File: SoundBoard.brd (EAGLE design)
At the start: 14.2 x 23.4 mm, 17 parts, among them IC1 LMV324, U1 ADMP401

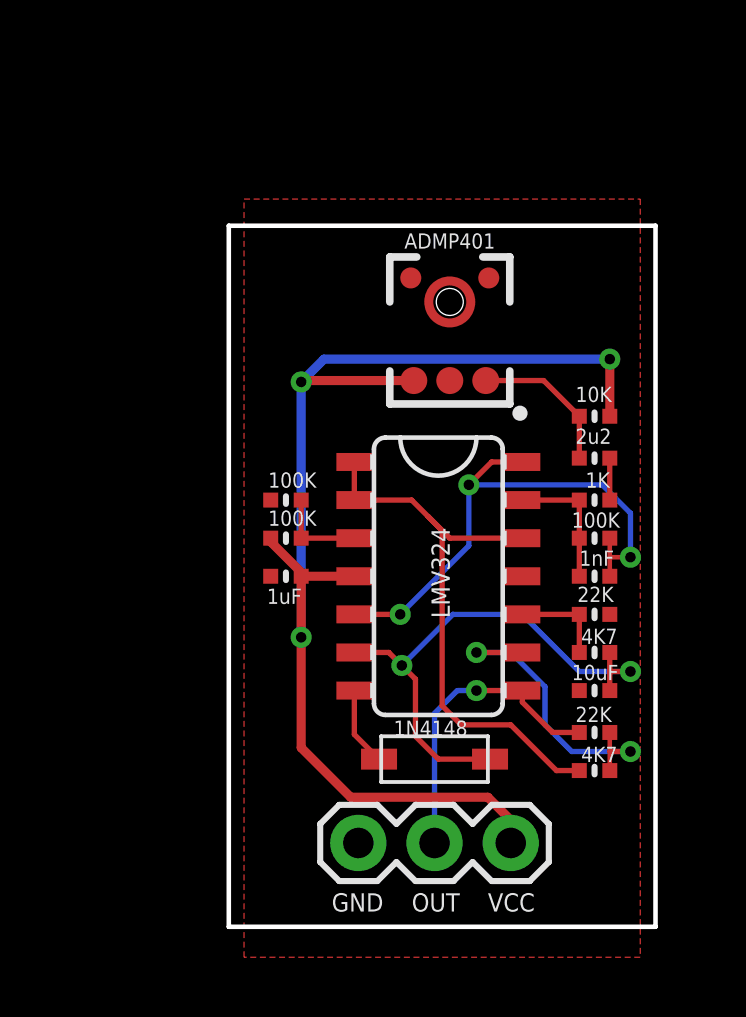
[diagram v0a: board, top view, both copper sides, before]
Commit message: v2 - updated OPAMP to LM324QT
- rerouted traces to accomodate for new QFN part
- Added electret microphone pins to test both
- rearranged some parts
- increased board dimensions slightly
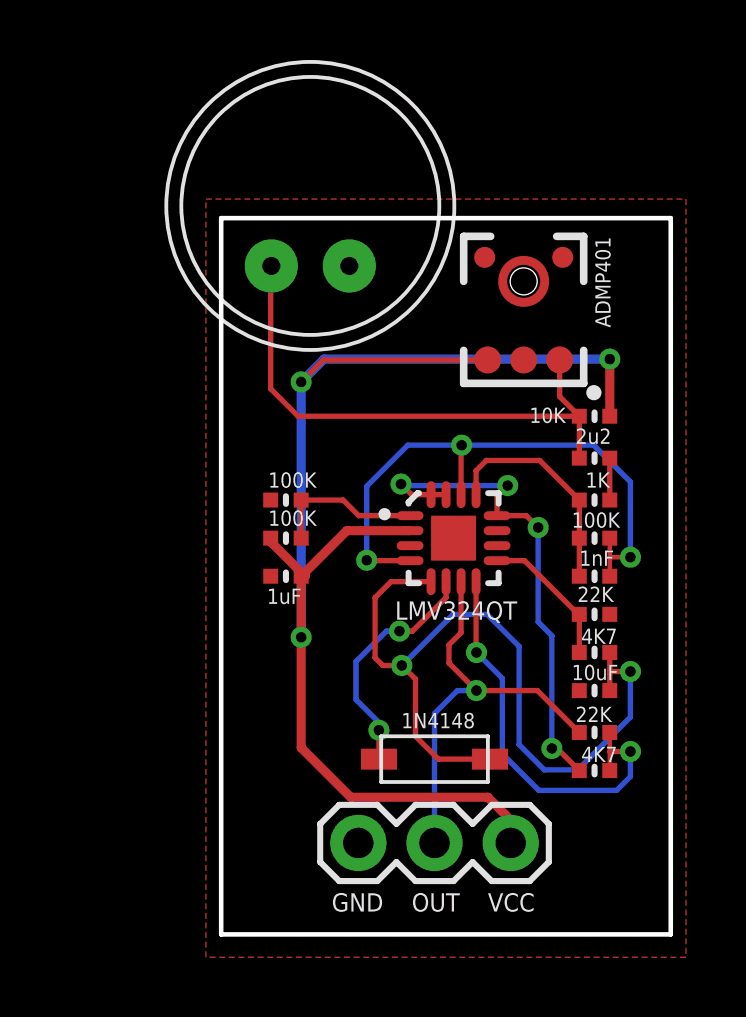
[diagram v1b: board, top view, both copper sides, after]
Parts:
- removed IC1: LMV324, SparkFun-AnalogIC:SO014
- added Q1: (no value), adafruit:9.7ELECTRET
- added U$1: LMV324QT, LMV324:QFN-16_3X3
- moved U1 2.56 mm to (12.9, 23.8)
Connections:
- net AMP: now also U$1.14, U$1.4; no longer IC1.14, IC1.5
- net GND: now also Q1.-, U$1.11; no longer IC1.11
- net N$2: now also U$1.13; no longer IC1.13
- net N$3: now also Q1.+
- net N$4: now also U$1.9; no longer IC1.10
- net N$5: now also U$1.8; no longer IC1.9
- net N$6: now also U$1.6; no longer IC1.7
- net N$7: now also U$1.5; no longer IC1.6
- net N$9: now also U$1.1; no longer IC1.3
- net OUT: now also U$1.7; no longer IC1.8
- net VCC: now also U$1.2; no longer IC1.4
- net VCC/2: now also U$1.12, U$1.15, U$1.16; no longer IC1.1, IC1.12, IC1.2
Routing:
- net N$3: track 5.01 -> 18.3 mm
- net N$7: track 18.2 -> 27.0 mm
- net VCC: track 42.8 -> 48.1 mm
- net N$6: track 2.63 -> 7.98 mm, vias 0 -> 2
- net OUT: track 10.3 -> 14.2 mm
- net N$5: track 10.7 -> 13.9 mm
- net N$2: track 4.44 -> 7.47 mm
- net VCC/2: track 19.4 -> 16.7 mm, vias 0 -> 4
- net N$9: track 3.04 -> 5.12 mm
- net AMP: track 18.1 -> 19.9 mm
- net N$4: track 3.17 -> 4.77 mm
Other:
- board size 14.2 x 23.4 mm -> 15 x 23.9 mm
- board text added: "Sound Board v2"
- board text removed: "LMV324"
- board text removed: "Sound Board"

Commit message: v3 - replaced MEMS mic with electret mic (adjusted circuitry)
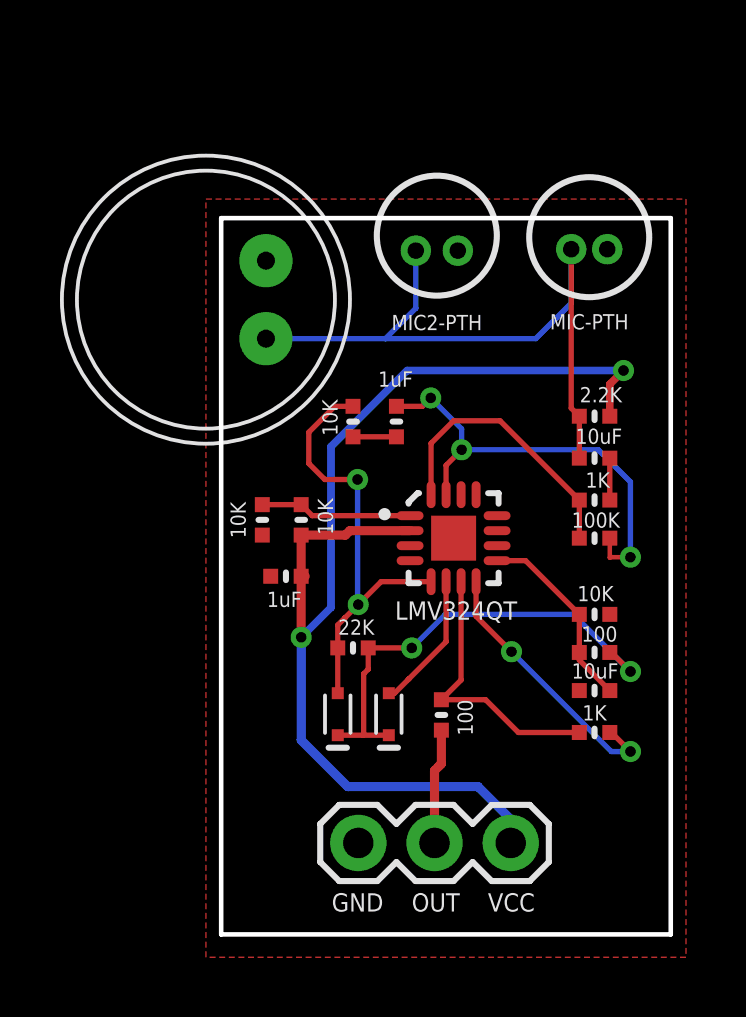
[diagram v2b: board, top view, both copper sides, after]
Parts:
- removed D1: 1N4148, adafruit:SOD-123
- removed U1: ADMP401, SparkFun-Sensors:ADMP401
- added D3, D4: 120mA/40V/370mV, SparkFun-DiscreteSemi:SOD-523
- added MK1: MIC2-PTH, CMC-4015-40P:MICROPHONE-PTH-4.0MM
- added MK2: MIC-PTH, TOM-1545P-R:MICROPHONE-PTH-4.0MM
- added R10: 10K, Adafruit PowerBoost 1000C Rev B:MICROBUILDER__0402MP
- added R11: 22K, Adafruit PowerBoost 1000C Rev B:MICROBUILDER__0402MP
- C1: value 2u2 -> 10uF
- C2: value 1nF -> 1uF
- R2: value 10K -> 2.2K
- R4, R6: value 4K7 -> 100
- R5: value 22K -> 10K
- R7: value 22K -> 1K
- R8, R9: value 100K -> 10K
- moved C2 8.38 mm to (8.64, 19.1), turned to 270 degrees
- moved R6 5.43 mm to (10.1, 9.35), turned to 90 degrees
- moved Q1 4.68 mm to (2.29, 23.2), turned to 270 degrees
- moved R8 1.00 mm to (4.17, 15.8), turned to 90 degrees
- moved R9 0.83 mm to (5.46, 15.8), turned to 270 degrees
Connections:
- removed net N$3: C1.1, Q1.+, R2.1, U1.1
- new net N$10: C1.1, MK1.OUT, MK2.OUT, Q1.+, R2.1
- new net N$8: C2.2, R10.2
- new net _OUT: R6.2, R7.1, U$1.7
- net AMP: now also C2.1, U$1.15; no longer C2.2, U$1.14, U$1.4
- net GND: now also MK1.GND, MK2.GND, R8.1, U$1.4; no longer R9.2, U1.2, U1.4, U1.6
- net N$2: now also U$1.16; no longer C2.1, U$1.13
- net N$4: now also D4.A, U$1.6; no longer R4.2, R5.2, U$1.9
- net N$5: no longer R6.1
- net N$6: now also D3.A, R10.1, R11.2, U$1.5; no longer D1.A, U$1.6
- net N$7: now also D3.C, D4.C, R11.1; no longer C3.2, D1.C, U$1.5
- net N$9: now also C3.2, R4.2, R5.2, U$1.9; no longer R8.2, R9.1, U$1.1
- net OUT: now also R6.1; no longer R7.1, U$1.7
- net VCC: now also R9.2; no longer R8.1, U1.5
- net VCC/2: now also R8.2, R9.1, U$1.1; no longer R6.2, U$1.12, U$1.15, U$1.16
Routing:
- net N$10: track 0.00 -> 22.9 mm
- net N$3: track 18.3 -> 0.00 mm
- net VCC/2: track 16.7 -> 5.08 mm, vias 4 -> 0
- net N$7: track 27.0 -> 15.6 mm
- net OUT: track 14.2 -> 4.00 mm, vias 1 -> 0
- net VCC: track 48.1 -> 38.8 mm, vias 3 -> 2
- net _OUT: track 0.00 -> 9.26 mm
- net N$6: track 7.98 -> 14.9 mm
- net AMP: track 19.9 -> 15.0 mm
- net N$5: track 13.9 -> 9.12 mm
- net N$2: track 7.47 -> 9.33 mm
- net N$8: track 0.00 -> 1.45 mm
- net N$9: track 5.12 -> 6.44 mm
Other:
- board text added: "Sound Board v3"
- board text removed: "Sound Board v2"
